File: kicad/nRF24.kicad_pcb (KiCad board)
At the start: 2 copper layers, 50 x 30 mm, 40 parts, among them J1 Conn_01x08, J2 Conn_Coaxial, U1 nRF24L01P, U2 TLV75733PDBV, U3 RFX2401C, X1 16MHz

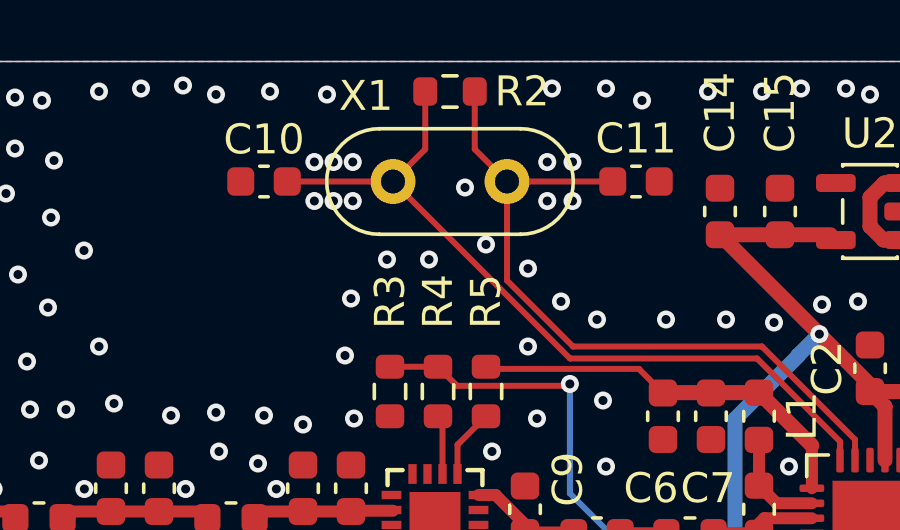
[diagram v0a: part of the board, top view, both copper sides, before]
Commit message: change crystal footprint
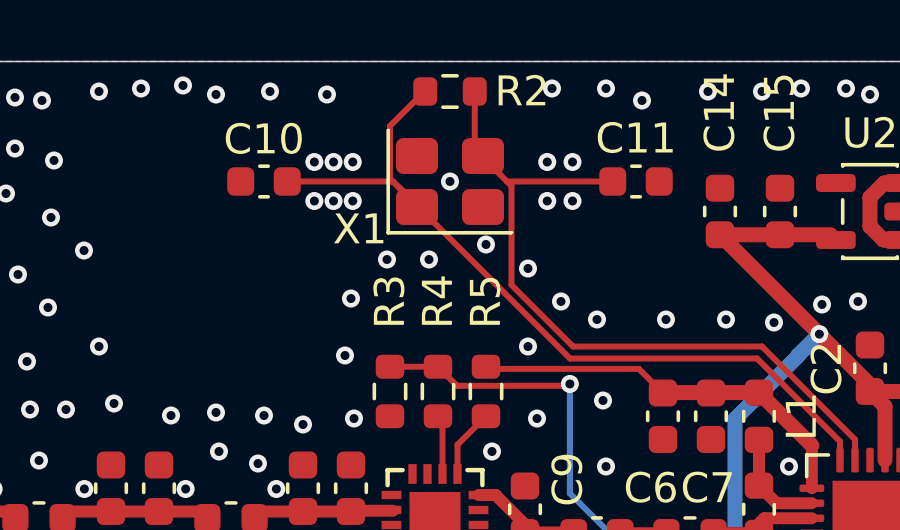
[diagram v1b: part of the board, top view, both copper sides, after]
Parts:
- X1: footprint Crystal:Crystal_HC52-U_Vertical -> Crystal:Crystal_SMD_3225-4Pin_3.2x2.5mm
- moved X1 1.90 mm to (56.0, 34.0)
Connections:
- X1 pad 2: XTAL_P -> GND
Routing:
- net XTAL_N: track 26.1 -> 28.2 mm
